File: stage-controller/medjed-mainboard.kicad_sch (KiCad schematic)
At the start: 44 parts, among them J1 Barrel_Jack, J2 ESTOP terminal, J3 Conn_01x04_Pin, SW2 ESTOP switch, U1 P78E-1000, U10 TCAN330, U11 teensy 4.1, U12 MIC5317-3.3, U13 MIC5317-1.8

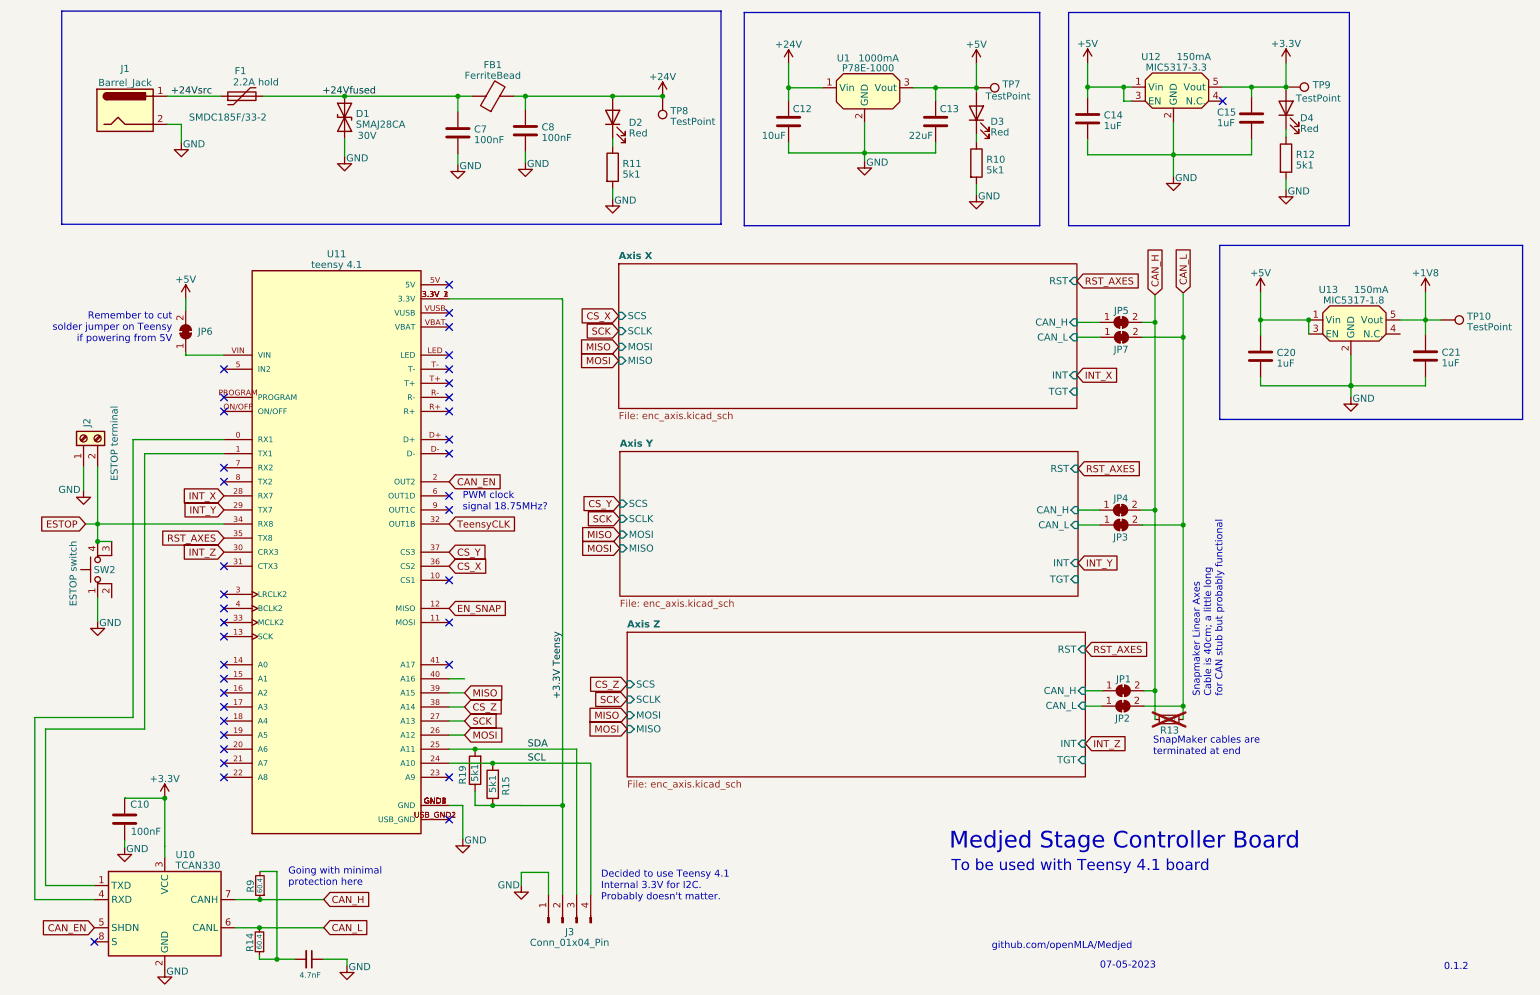
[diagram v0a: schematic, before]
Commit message: Fix Clock pin and MISO/MOSI error
The TeensyCLK signal was routed to a pin on the Teensy 4.1 that did not support PWM. Now fixed. MOSI and MISO of SPI interface were flipped around by mistake. Now in correct orientation and should allow SPI communication (tested with messy wiring).
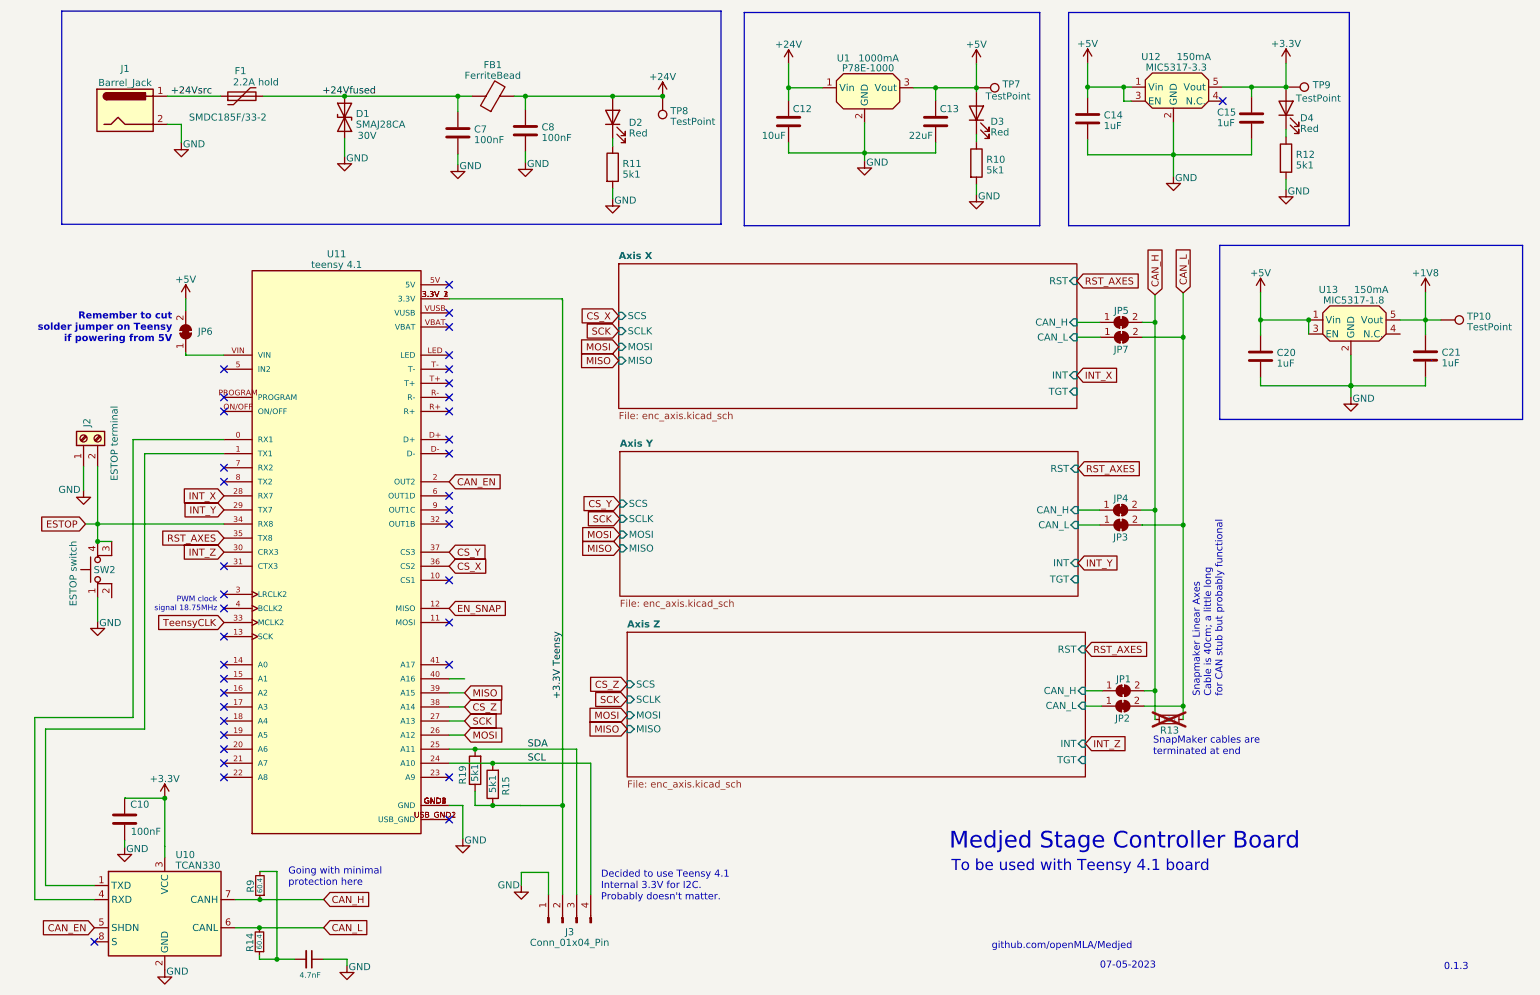
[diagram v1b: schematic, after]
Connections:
- net TeensyCLK: now also U11.33 (MCLK2); no longer U11.32 (OUT1B)
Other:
- note added: "0.1.3"
- note added: "PWM clock signal 18.75MHz"
- note removed: "0.1.2"
- note removed: "PWM clock signal 18.75MHz?"

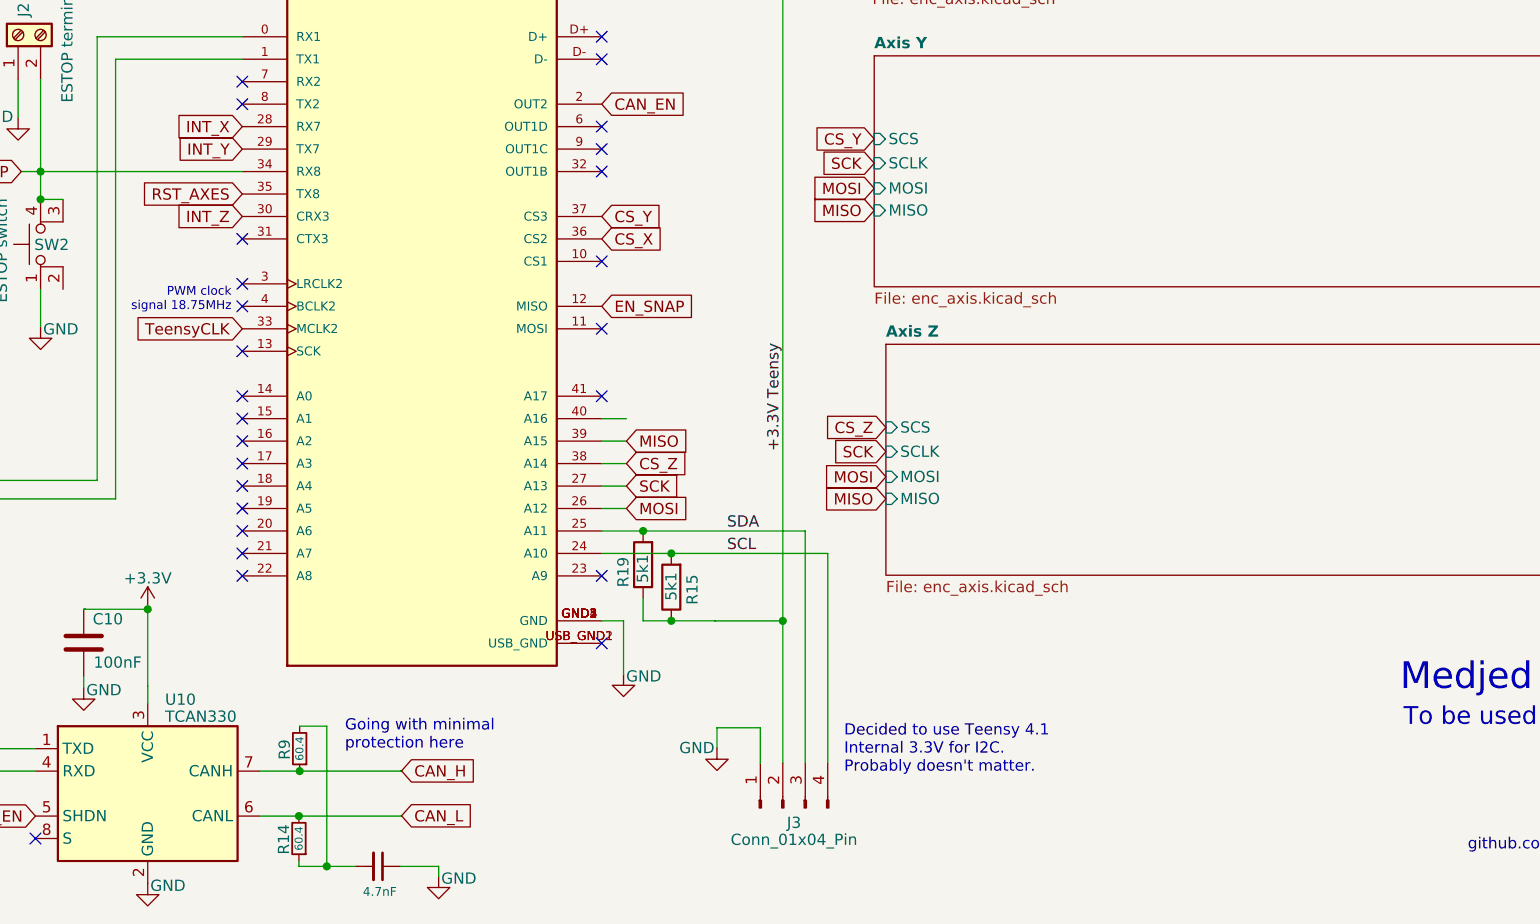
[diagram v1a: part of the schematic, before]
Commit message: Removed differential line receivers
During design of the board I did not realise that the TMC4631 already has this built in (I had different motion controllers before). So the AM26LS32A ICs should not be needed. Removed these and rerouted the board.
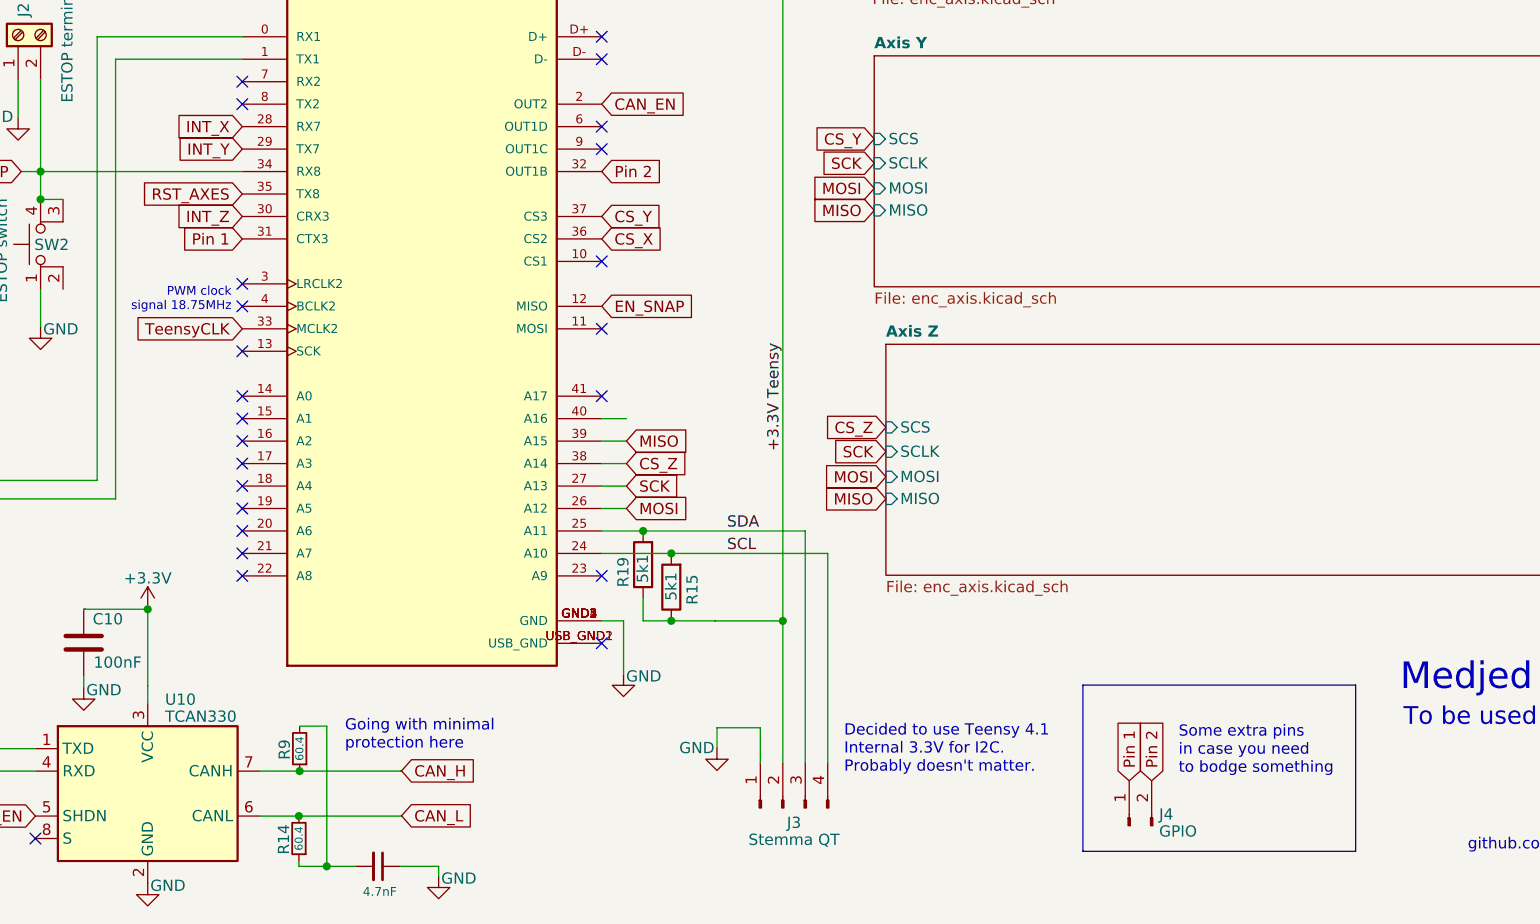
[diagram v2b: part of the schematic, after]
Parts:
- added J4: GPIO, Connector_PinSocket_2.54mm:PinSocket_1x02_P2.54mm_Vertical, symbol Connector:Conn_01x02_Pin
- J3: value Conn_01x04_Pin -> Stemma QT
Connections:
- net Pin 1: now reaches U11.31 (CTX3)
- net Pin 1: now also J4.1 (Pin_1)
- net Pin 2: now reaches U11.32 (OUT1B)
- net Pin 2: now also J4.2 (Pin_2)
- no-connect marks 38 -> 36
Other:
- note added: "Some extra pins in case you need to bodge something"
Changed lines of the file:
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@@
   (no_connect (at 89.1032 159.258))
   (no_connect (at 25.0698 188.9506))
-  (no_connect (at 48.4632 121.158))
   (no_connect (at 89.1032 98.298))
   (no_connect (at 48.4632 103.378))
@@
   (no_connect (at 48.4632 154.178))
   (no_connect (at 89.1032 110.998))
-  (no_connect (at 89.1032 113.538))
   (wire (pts (xy 100.838 36.322) (xy 102.87 36.322))
     (stroke (width 0) (type default))
@@
   (wire (pts (xy 23.114 103.1748) (xy 23.114 107.442))
     (stroke (width 0) (type default))
+  )
+  (rectangle (start 143.51 171.6024) (end 174.3456 190.3984)
+    (stroke (width 0) (type default))
+    (fill (type none))
   )
   (rectangle (start 19.177 20.955) (end 138.176 59.436)
@@
   (text "github.com/openMLA/Medjed" (at 187.0202 190.4746 0)
     (effects (font (size 1.27 1.27)) (justify left bottom) (href "https://github.com/openMLA/Medjed"))
+  )
+  (text "Some extra pins\nin case you need\nto bodge something"
+    (at 154.3304 181.8132 0)
+    (effects (font (size 1.27 1.27)) (justify left bottom))
   )
   (text "07-05-2023" (at 206.5528 194.0052 0)
@@
     )
   )
+  (global_label "Pin 2" (shape input) (at 151.2824 182.4228 90) (fields_autoplaced)
+    (effects (font (size 1.27 1.27)) (justify left))
+    (property "Intersheetrefs" "${INTERSHEET_REFS}" (at 151.2824 174.3161 90)
+      (effects (font (size 1.27 1.27)) (justify left) hide)
+    )
+  )
   (global_label "SCK" (shape input) (at 91.8972 149.098 0) (fields_autoplaced)
     (effects (font (size 1.27 1.27)) (justify left))
@@
     )
   )
+  (global_label "Pin 1" (shape input) (at 148.7424 182.4228 90) (fields_autoplaced)
+    (effects (font (size 1.27 1.27)) (justify left))
+    (property "Intersheetrefs" "${INTERSHEET_REFS}" (at 148.7424 174.3161 90)
+      (effects (font (size 1.27 1.27)) (justify left) hide)
+    )
+  )
   (global_label "CS_Z" (shape input) (at 91.8972 146.558 0) (fields_autoplaced)
     (effects (font (size 1.27 1.27)) (justify left))
@@
     )
   )
+  (global_label "Pin 1" (shape input) (at 48.4632 121.158 180) (fields_autoplaced)
+    (effects (font (size 1.27 1.27)) (justify right))
+    (property "Intersheetrefs" "${INTERSHEET_REFS}" (at 40.3565 121.158 0)
+      (effects (font (size 1.27 1.27)) (justify right) hide)
+    )
+  )
   (global_label "MISO" (shape input) (at 119.9134 117.9322 180) (fields_autoplaced)
     (effects (font (size 1.27 1.27)) (justify right))
@@
     (effects (font (size 1.27 1.27)) (justify left))
     (property "Intersheetrefs" "${INTERSHEET_REFS}" (at 75.3648 181.3052 0)
+      (effects (font (size 1.27 1.27)) (justify left) hide)
+    )
+  )
+  (global_label "Pin 2" (shape input) (at 89.1032 113.538 0) (fields_autoplaced)
+    (effects (font (size 1.27 1.27)) (justify left))
+    (property "Intersheetrefs" "${INTERSHEET_REFS}" (at 97.2099 113.538 0)
       (effects (font (size 1.27 1.27)) (justify left) hide)
     )
@@
     )
   )
+  (symbol (lib_id "Connector:Conn_01x02_Pin") (at 148.7424 187.5028 90) (unit 1)
+    (in_bom yes) (on_board yes) (dnp no) (fields_autoplaced)
+    (property "Reference" "J4" (at 152.1206 186.2241 90)
+      (effects (font (size 1.27 1.27)) (justify right))
+    )
+    (property "Value" "GPIO" (at 152.1206 188.1451 90)
+      (effects (font (size 1.27 1.27)) (justify right))
+    )
+    (property "Footprint" "Connector_PinSocket_2.54mm:PinSocket_1x02_P2.54mm_Vertical" (at 148.7424 187.5028 0)
+      (effects (font (size 1.27 1.27)) hide)
+    )
+    (property "Datasheet" "~" (at 148.7424 187.5028 0)
+      (effects (font (size 1.27 1.27)) hide)
+    )
+    (pin "1")
+    (pin "2")
+    (instances
+      (project "medjed-mainboard"
+        (path "/27a9022c-c259-44d6-8dfc-ca2dec4f8d18"
+          (reference "J4") (unit 1)
+        )
+      )
+    )
+  )
   (symbol (lib_id "Switch:SW_MEC_5E") (at 28.194 121.7676 90) (unit 1)
     (in_bom yes) (on_board yes) (dnp no)
@@
       (effects (font (size 1.27 1.27)))
     )
-    (property "Value" "Conn_01x04_Pin" (at 110.8456 189.0889 90)
-      (effects (font (size 1.27 1.27)))
-    )
+    (property "Value" "Stemma QT" (at 110.8456 189.0889 90)
+      (effects (font (size 1.27 1.27)))
+    )
